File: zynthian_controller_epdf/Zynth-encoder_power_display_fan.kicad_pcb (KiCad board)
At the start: 2 copper layers, 65 x 56 mm, 41 parts, among them J3 40HAT, Q1 DMG2305UX, Q2 DMMT5401, Q3 AOD4184A, U2 CAT24C32, U3 MCP23017_SS

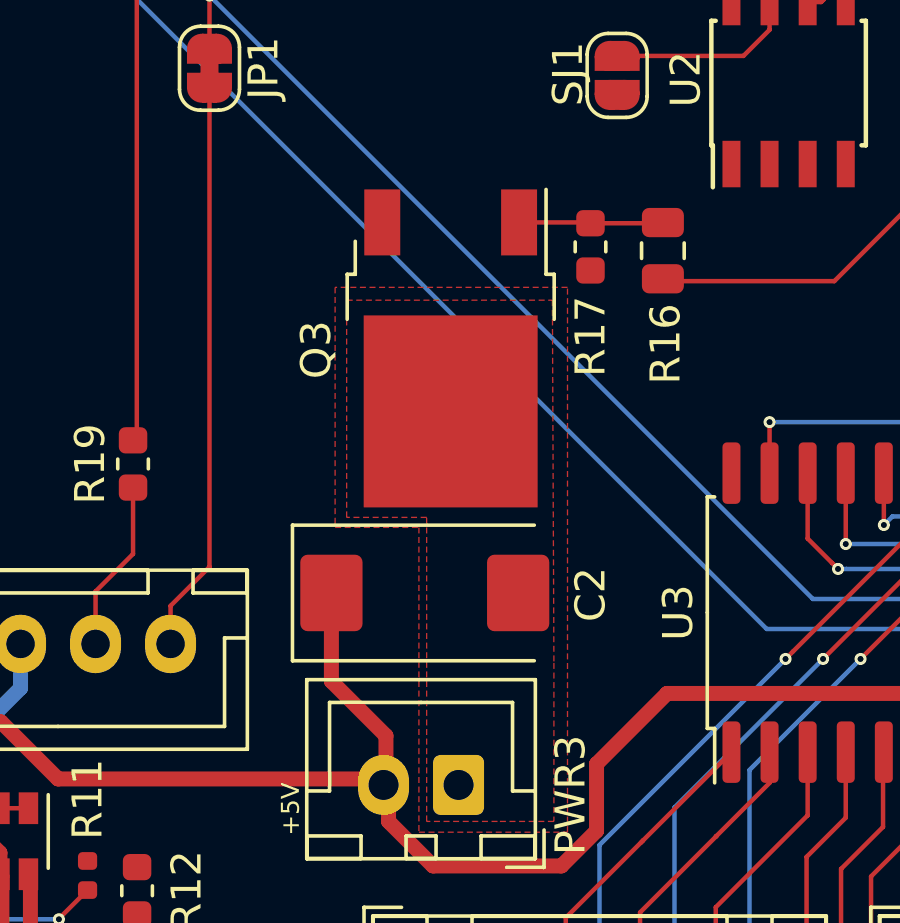
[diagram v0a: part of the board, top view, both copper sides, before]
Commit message: Corrections before production.
Optimized and tested for submit
Manually corrected R12,18,19 as well as pin 1 orientations.
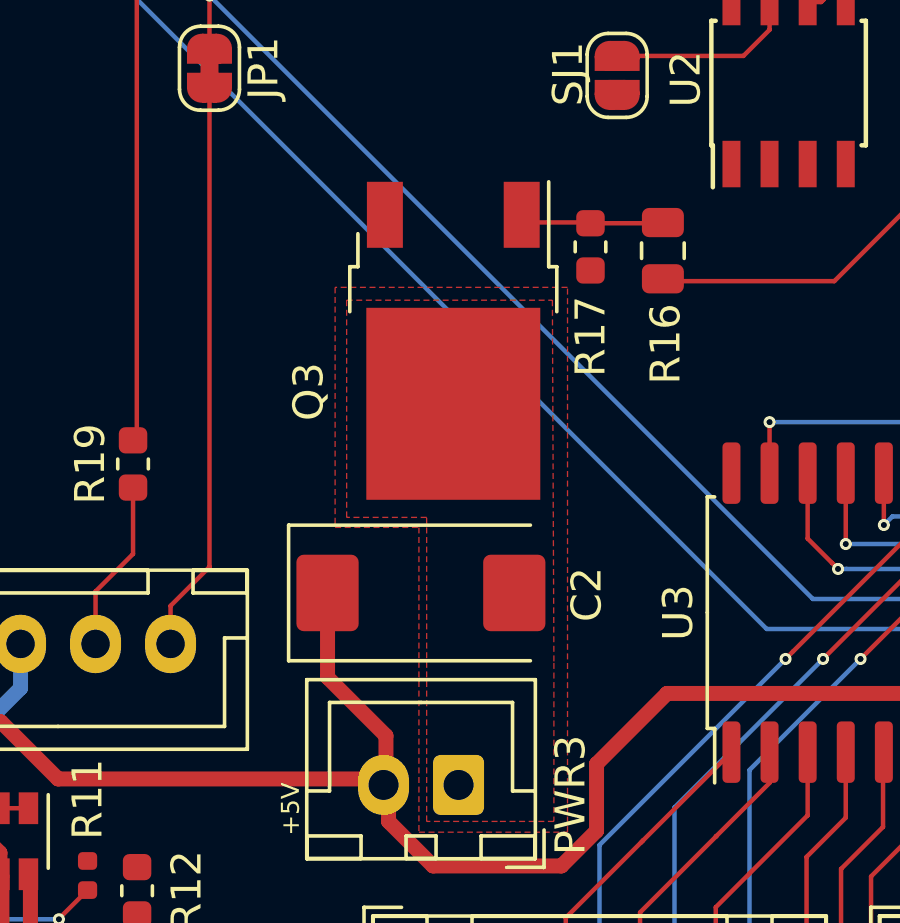
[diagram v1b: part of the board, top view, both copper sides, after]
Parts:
- Q3: value AOD4184A -> Q_NMOS_GDS
- moved Q3 0.27 mm to (106.4, 83.4)
- moved C2 0.13 mm to (105.3, 91.8)
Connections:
- J3 pad 10: (no net) -> Net-(J3-Pad10)
- J3 pad 12: (no net) -> Net-(J3-Pad12)
- J3 pad 13: (no net) -> Net-(J3-Pad13)
- J3 pad 15: (no net) -> Net-(J3-Pad15)
- J3 pad 16: (no net) -> Net-(J3-Pad16)
- J3 pad 17: (no net) -> Net-(J3-Pad17)
- J3 pad 18: (no net) -> Net-(J3-Pad18)
- J3 pad 19: (no net) -> Net-(J3-Pad19)
- J3 pad 21: (no net) -> Net-(J3-Pad21)
- J3 pad 22: (no net) -> Net-(J3-Pad22)
- J3 pad 23: (no net) -> Net-(J3-Pad23)
- J3 pad 24: (no net) -> Net-(J3-Pad24)
- J3 pad 26: (no net) -> Net-(J3-Pad26)
- J3 pad 29: (no net) -> Net-(J3-Pad29)
- J3 pad 31: (no net) -> Net-(J3-Pad31)
- J3 pad 35: (no net) -> Net-(J3-Pad35)
- J3 pad 38: (no net) -> Net-(J3-Pad38)
- J3 pad 40: (no net) -> Net-(J3-Pad40)
- J3 pad 7: (no net) -> Net-(J3-Pad7)
- J3 pad 8: (no net) -> Net-(J3-Pad8)
- U3 pad 11: (no net) -> Net-(U3-Pad11)
- U3 pad 14: (no net) -> Net-(U3-Pad14)
- U3 pad 28: (no net) -> /GSW4

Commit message: Final Changes before production
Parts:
- added R20: 100K, Resistor_SMD:R_0603_1608Metric, F.Cu at (130.9, 100.1)
- C2: footprint Capacitor_Tantalum_SMD:CP_EIA-7343-30_AVX-N -> Capacitor_Tantalum_SMD:CP_EIA-3528-15_AVX-H
- R11: footprint Resistor_SMD:R_0402_1005Metric -> Resistor_SMD:R_0603_1608Metric
- R18, R19: value 1k -> 1K
- moved R12 0.53 mm to (95.9, 101.2)
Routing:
- net /P5V_HAT: track 149.1 -> 148.6 mm

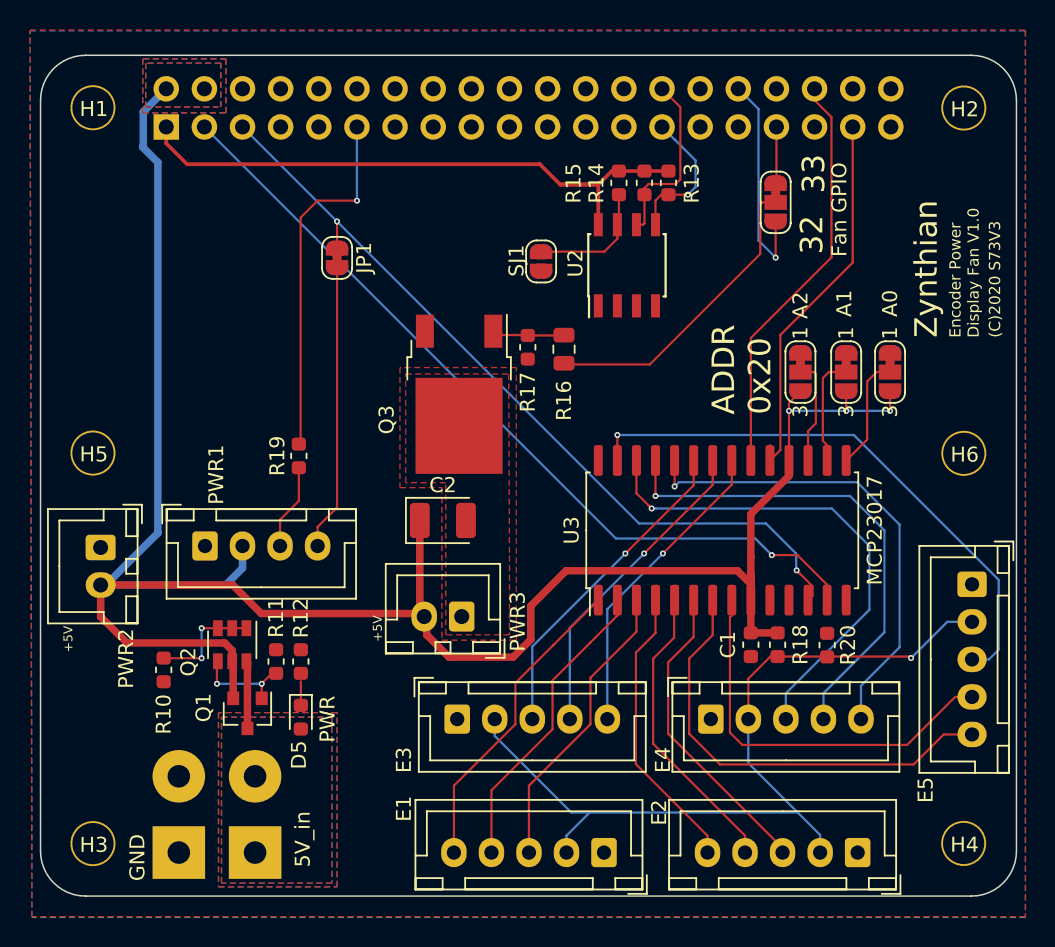
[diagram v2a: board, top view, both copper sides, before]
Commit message: Move GPIOs change act_led R19 220 Ohm
Based upon various descriptions of Pi LED, and 3.3V Decided to use
220 Ohm resistor, rather than 0Ohm or 1K. 603 pad is possible to
replace resistor if required. Should be low enough R to work on all LED

Rework GPIO lines to use lines marked not in use by Ozz display in
hopes of keeping this compatible for most folks.

It will be possible to mag wire rework and epoxy glue to do a test
upgrade before the next rev of HW. Should even be clean and tidy.
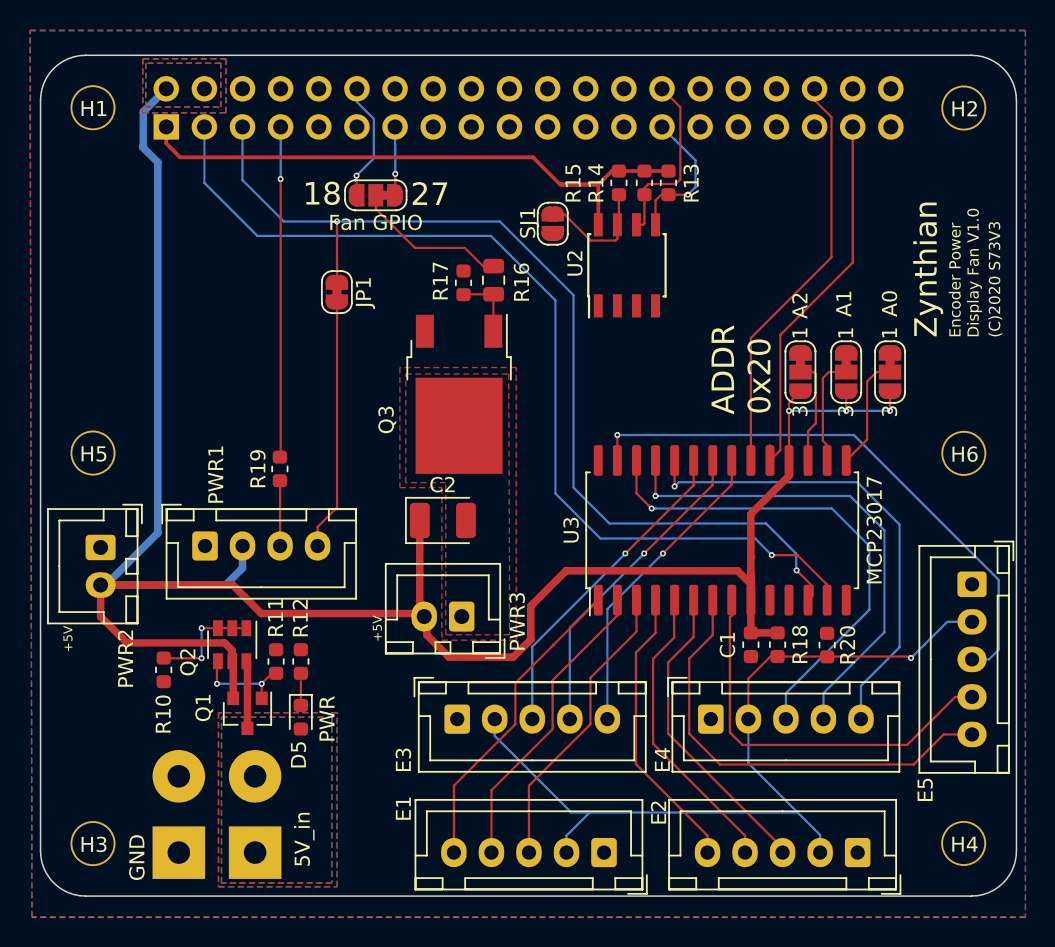
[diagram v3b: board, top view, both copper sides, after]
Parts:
- R19: value 1K -> 200
- moved FAN1 26.6 mm to (100.9, 70.1), turned to 180 degrees
- moved R16 6.56 mm to (108.7, 75.8), turned to 270 degrees
- moved R17 6.06 mm to (106.7, 76.0), turned to 90 degrees
- moved SJ1 2.63 mm to (112.7, 72.0)
- moved JP1 2.28 mm to (98.3, 76.6)
- moved R19 1.53 mm to (94.5, 88.4)
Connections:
- net /GSW4 renamed Net-(U3-Pad28)
- J3 pad 11: /ACT_LED -> Net-(J3-Pad11)
- J3 pad 12: Net-(J3-Pad12) -> /PWM_FAN_2
- J3 pad 13: Net-(J3-Pad13) -> /PWM_FAN_1
- J3 pad 32: /PWM_FAN_2 -> Net-(J3-Pad32)
- J3 pad 33: /PWM_FAN_1 -> Net-(J3-Pad33)
- J3 pad 7: Net-(J3-Pad7) -> /ACT_LED
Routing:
- net /SCK: track 53.8 -> 66.0 mm
- net Net-(FAN1-Pad2): track 20.5 -> 10.3 mm
- net /SDA: track 55.1 -> 64.9 mm
- net /PWM_FAN_2: track 14.7 -> 8.04 mm
- net Net-(JP1-Pad2): track 18.8 -> 16.8 mm
- net /ACT_LED: track 23.9 -> 22.0 mm
- net Net-(PWR1-Pad3): track 5.73 -> 4.35 mm
- net /PWM_FAN_1: track 3.74 -> 4.61 mm, vias 0 -> 1
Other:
- board text added: "18"
- board text added: "27"
- board text removed: "32"
- board text removed: "33"
